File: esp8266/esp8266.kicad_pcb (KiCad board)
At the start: 2 copper layers, 50 x 50 mm, 29 parts, among them J1 Screw_Terminal_1x02, J2 Screw_Terminal_1x03, P1 CONN_02X04, P2 CONN_01X03, P3 CONN_01X03, P4 CONN_01X03, P5 CONN_01X03, P6 CONN_01X03, U1 LM1117-3.3

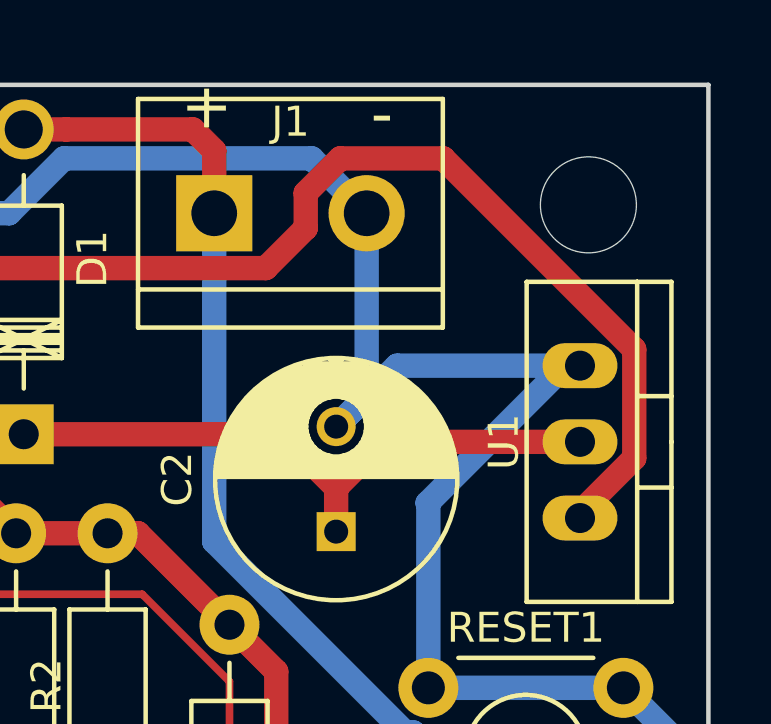
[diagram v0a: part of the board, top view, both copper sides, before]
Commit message: changed to LD1117
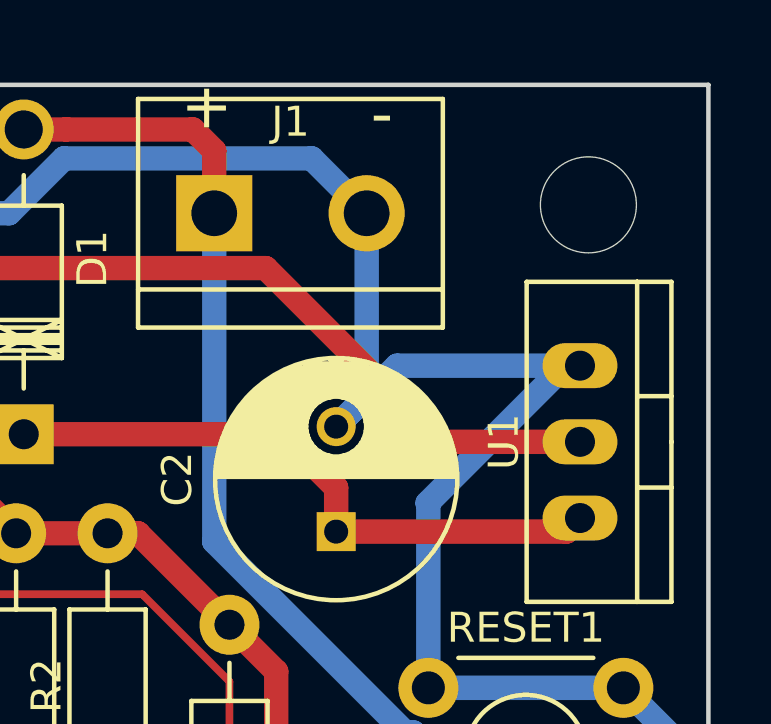
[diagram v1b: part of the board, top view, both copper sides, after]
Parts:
- U1: value LM1117-3.3 -> LD1117S33TR
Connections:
- U1 pad 2: VDD -> +3V3
- U1 pad 3: +3V3 -> VDD
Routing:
- net +3V3: track 142.2 -> 131.6 mm
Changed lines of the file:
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@@
     (thickness 1.6)
     (drawings 27)
-    (tracks 212)
+    (tracks 206)
     (zones 0)
     (modules 29)
@@
     (visible_elements FFFFFF7F)
     (pcbplotparams
-      (layerselection 0x090f0_ffffffff)
+      (layerselection 0x010f0_ffffffff)
       (usegerberextensions true)
       (excludeedgelayer true)
@@
       (effects (font (size 1 1) (thickness 0.15)))
     )
-    (fp_text value LM1117-3.3 (at 0 3.81 270) (layer F.Fab)
+    (fp_text value LD1117S33TR (at 0 3.81 270) (layer F.Fab)
       (effects (font (size 1 1) (thickness 0.15)))
     )
@@
     (fp_line (start 0 -3.048) (end 5.334 -3.048) (layer F.SilkS) (width 0.15))
     (pad 2 thru_hole oval (at 0 0) (size 2.49936 1.50114) (drill 1.00076) (layers *.Cu *.Mask)
+      (net 1 +3V3))
+    (pad 1 thru_hole oval (at -2.54 0) (size 2.49936 1.50114) (drill 1.00076) (layers *.Cu *.Mask)
+      (net 2 GND))
+    (pad 3 thru_hole oval (at 2.54 0) (size 2.49936 1.50114) (drill 1.00076) (layers *.Cu *.Mask)
       (net 6 VDD))
-    (pad 1 thru_hole oval (at -2.54 0) (size 2.49936 1.50114) (drill 1.00076) (layers *.Cu *.Mask)
-      (net 2 GND))
-    (pad 3 thru_hole oval (at 2.54 0) (size 2.49936 1.50114) (drill 1.00076) (layers *.Cu *.Mask)
-      (net 1 +3V3))
     (model TO_SOT_Packages_THT.3dshapes/TO-220_Neutral123_Vertical.wrl
       (at (xyz 0 0 0))
@@
   (gr_line (start 134.62 114.3) (end 184.62 114.3) (angle 90) (layer Edge.Cuts) (width 0.15))
   (segment (start 161.544 104.14) (end 161.798 104.14) (width 0.254) (layer F.Cu) (net 0))
+  (segment (start 169.865041 70.408801) (end 175.65624 76.2) (width 0.8128) (layer F.Cu) (net 1))
+  (segment (start 175.65624 76.2) (end 180.34 76.2) (width 0.8128) (layer F.Cu) (net 1))
   (segment (start 168.91 109.728) (end 169.773599 108.864401) (width 0.8128) (layer F.Cu) (net 1))
   (segment (start 169.773599 108.864401) (end 171.064799 108.864401) (width 0.8128) (layer F.Cu) (net 1))
@@
   (segment (start 149.707601 70.408801) (end 147.8788 68.58) (width 0.8128) (layer F.Cu) (net 1))
   (segment (start 147.8788 68.58) (end 145.796 68.58) (width 0.8128) (layer F.Cu) (net 1))
-  (segment (start 171.196 69.077842) (end 169.865041 70.408801) (width 0.8128) (layer F.Cu) (net 1))
   (segment (start 156.260799 70.408801) (end 151.638 75.0316) (width 0.8128) (layer F.Cu) (net 1))
   (segment (start 151.638 75.0316) (end 151.638 75.184) (width 0.8128) (layer F.Cu) (net 1))
-  (segment (start 171.196 67.905374) (end 171.196 69.077842) (width 0.8128) (layer F.Cu) (net 1))
-  (segment (start 180.34 78.74) (end 180.34 78.550852) (width 0.8128) (layer F.Cu) (net 1))
-  (segment (start 180.34 78.550852) (end 182.14849 76.742362) (width 0.8128) (layer F.Cu) (net 1))
-  (segment (start 182.14849 76.742362) (end 182.14849 73.117638) (width 0.8128) (layer F.Cu) (net 1))
-  (segment (start 182.14849 73.117638) (end 175.782051 66.751199) (width 0.8128) (layer F.Cu) (net 1))
-  (segment (start 172.350175 66.751199) (end 171.196 67.905374) (width 0.8128) (layer F.Cu) (net 1))
-  (segment (start 175.782051 66.751199) (end 172.350175 66.751199) (width 0.8128) (layer F.Cu) (net 1))
   (segment (start 181.864 93.036) (end 181.864 95.228974) (width 0.8128) (layer B.Cu) (net 2))
   (segment (start 181.864 95.228974) (end 183.422801 96.787775) (width 0.8128) (layer B.Cu) (net 2))
@@
   (segment (start 167.513001 108.584999) (end 168.046401 108.051599) (width 0.254) (layer F.Cu) (net 5))
   (segment (start 168.046401 108.051599) (end 168.91 107.188) (width 0.254) (layer F.Cu) (net 5))
+  (segment (start 172.212 79.192) (end 179.888 79.192) (width 0.8128) (layer F.Cu) (net 6))
+  (segment (start 179.888 79.192) (end 180.34 78.74) (width 0.8128) (layer F.Cu) (net 6))
+  (segment (start 180.34 78.74) (end 180.34 78.550852) (width 0.8128) (layer F.Cu) (net 6))
   (segment (start 172.212 79.192) (end 172.212 77.7292) (width 0.8128) (layer F.Cu) (net 6))
-  (segment (start 172.212 77.7292) (end 173.7412 76.2) (width 0.8128) (layer F.Cu) (net 6))
-  (segment (start 173.7412 76.2) (end 178.27752 76.2) (width 0.8128) (layer F.Cu) (net 6))
-  (segment (start 178.27752 76.2) (end 180.34 76.2) (width 0.8128) (layer F.Cu) (net 6))
   (segment (start 161.798 75.946) (end 170.4288 75.946) (width 0.8128) (layer F.Cu) (net 6))
   (segment (start 170.4288 75.946) (end 172.212 77.7292) (width 0.8128) (layer F.Cu) (net 6))
